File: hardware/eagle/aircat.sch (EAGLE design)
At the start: 180 parts, among them CON1 A10_OLINUXINO_LIME_SHIELD_TEM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, CON2 ANALOG_OUT, CON3 ANALOG_IN, CON4 SPDIF_OUT, U1 PCM3168A, U2 OPA1644AIPW, U3 OPA1644AIPW, U4 OPA1644AIPW, U6 LM2662M

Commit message: added test points for unused data lines
fix #7
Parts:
- added DOUT2(NC), DOUT3(NC): TPTP10SQ, testpad:TPTP10SQ
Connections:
- new net DOUT2(NC): CON1_GPIO-3.20, DOUT2(NC).TP
- new net DOUT3(NC): CON1_GPIO-3.18, DOUT3(NC).TP
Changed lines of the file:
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@@
 <attribute name="TP_SIGNAL_NAME" value=""/>
 </part>
+<part name="DOUT2(NC)" library="testpad" deviceset="TP" device="TP10SQ" value="TPTP10SQ">
+<attribute name="MF" value=""/>
+<attribute name="MPN" value=""/>
+<attribute name="OC_FARNELL" value="unknown"/>
+<attribute name="TP_SIGNAL_NAME" value=""/>
+</part>
+<part name="DOUT3(NC)" library="testpad" deviceset="TP" device="TP10SQ" value="TPTP10SQ">
+<attribute name="MF" value=""/>
+<attribute name="MPN" value=""/>
+<attribute name="OC_FARNELL" value="unknown"/>
+<attribute name="TP_SIGNAL_NAME" value=""/>
+</part>
 </parts>
 <sheets>
@@
 <attribute name="MPN" x="-238.76" y="-114.3" size="1.778" layer="96" rot="R90" display="off"/>
 </instance>
+<instance part="DOUT2(NC)" gate="G$1" x="-157.48" y="-27.94" smashed="yes" rot="R270">
+<attribute name="OC_FARNELL" x="-157.48" y="-27.94" size="1.778" layer="96" display="off"/>
+<attribute name="MF" x="-157.48" y="-27.94" size="1.778" layer="96" display="off"/>
+<attribute name="MPN" x="-157.48" y="-27.94" size="1.778" layer="96" display="off"/>
+<attribute name="NAME" x="-156.718" y="-28.956" size="1.778" layer="95"/>
+<attribute name="TP_SIGNAL_NAME" x="-158.75" y="-29.21" size="1.778" layer="97" rot="R270"/>
+</instance>
+<instance part="DOUT3(NC)" gate="G$1" x="-157.48" y="-30.48" smashed="yes" rot="R270">
+<attribute name="OC_FARNELL" x="-157.48" y="-30.48" size="1.778" layer="96" display="off"/>
+<attribute name="MF" x="-157.48" y="-30.48" size="1.778" layer="96" display="off"/>
+<attribute name="MPN" x="-157.48" y="-30.48" size="1.778" layer="96" display="off"/>
+<attribute name="NAME" x="-156.718" y="-31.496" size="1.778" layer="95"/>
+<attribute name="TP_SIGNAL_NAME" x="-158.75" y="-31.75" size="1.778" layer="97" rot="R270"/>
+</instance>
 </instances>
 <busses>
@@
 </segment>
 </net>
+<net name="DOUT2(NC)" class="0">
+<segment>
+<pinref part="CON1" gate="_GPIO-3" pin="20"/>
+<wire x1="-182.88" y1="-27.94" x2="-180.34" y2="-27.94" width="0.1524" layer="91"/>
+<label x="-180.34" y="-27.94" size="1.778" layer="95"/>
+</segment>
+<segment>
+<pinref part="DOUT2(NC)" gate="G$1" pin="TP"/>
+<wire x1="-160.02" y1="-27.94" x2="-162.56" y2="-27.94" width="0.1524" layer="91"/>
+</segment>
+</net>
+<net name="DOUT3(NC)" class="0">
+<segment>
+<pinref part="CON1" gate="_GPIO-3" pin="18"/>
+<wire x1="-182.88" y1="-30.48" x2="-180.34" y2="-30.48" width="0.1524" layer="91"/>
+<label x="-180.34" y="-30.48" size="1.778" layer="95"/>
+</segment>
+<segment>
+<pinref part="DOUT3(NC)" gate="G$1" pin="TP"/>
+<wire x1="-160.02" y1="-30.48" x2="-162.56" y2="-30.48" width="0.1524" layer="91"/>
+</segment>
+</net>

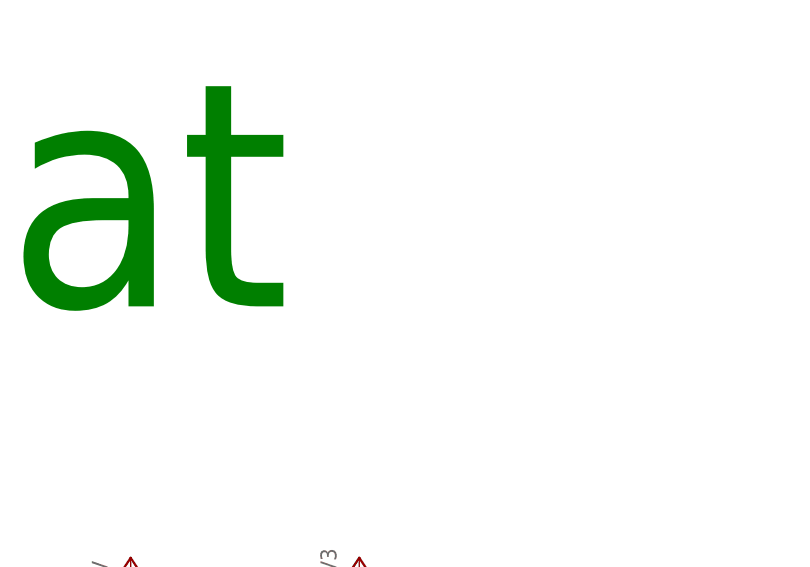
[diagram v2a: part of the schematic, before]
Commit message: added licence logo
fix #6
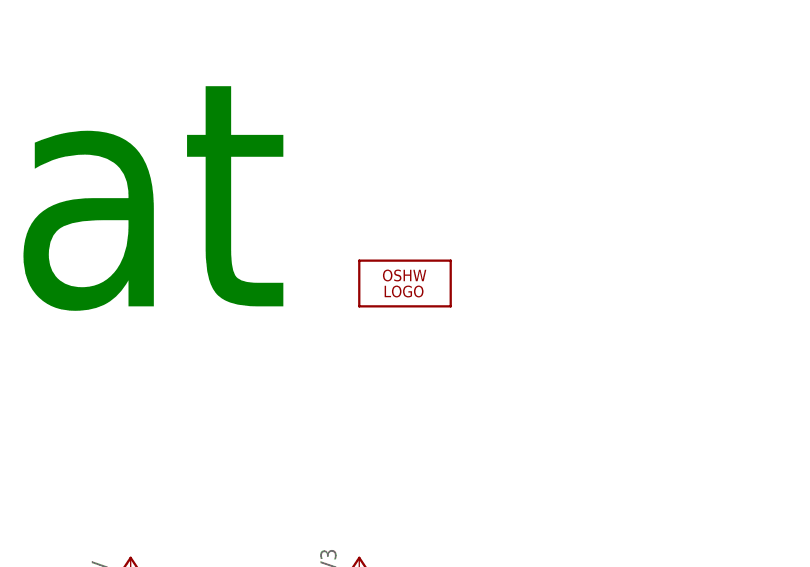
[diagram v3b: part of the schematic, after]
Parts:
- added LOGO1: OSHW_LOGO_FILLX0200-NT, ohw-logo:OSHW_LOGO_FILLX0200-NT
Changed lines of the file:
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@@
 <layer number="98" name="Guide" color="6" fill="1" visible="yes" active="yes"/>
 <layer number="100" name="Muster" color="7" fill="1" visible="no" active="no"/>
+<layer number="101" name="DRAWREF" color="11" fill="1" visible="no" active="yes"/>
+<layer number="102" name="Vscore" color="7" fill="1" visible="yes" active="yes"/>
+<layer number="103" name="tMap" color="7" fill="1" visible="yes" active="yes"/>
+<layer number="104" name="Name" color="16" fill="1" visible="yes" active="yes"/>
+<layer number="105" name="tPlate" color="7" fill="1" visible="yes" active="yes"/>
+<layer number="106" name="bPlate" color="7" fill="1" visible="yes" active="yes"/>
+<layer number="107" name="Crop" color="7" fill="1" visible="yes" active="yes"/>
+<layer number="116" name="Patch_BOT" color="9" fill="4" visible="yes" active="yes"/>
+<layer number="121" name="_tsilk" color="7" fill="1" visible="yes" active="yes"/>
+<layer number="122" name="_bsilk" color="7" fill="1" visible="yes" active="yes"/>
+<layer number="144" name="DrillLegend" color="7" fill="1" visible="no" active="yes"/>
+<layer number="151" name="HeatSink" color="7" fill="1" visible="yes" active="yes"/>
+<layer number="200" name="200bmp" color="1" fill="10" visible="no" active="yes"/>
+<layer number="201" name="201bmp" color="2" fill="10" visible="no" active="yes"/>
+<layer number="202" name="202bmp" color="3" fill="10" visible="no" active="yes"/>
+<layer number="203" name="203bmp" color="4" fill="10" visible="no" active="yes"/>
+<layer number="204" name="204bmp" color="5" fill="10" visible="no" active="yes"/>
+<layer number="205" name="205bmp" color="6" fill="10" visible="no" active="yes"/>
+<layer number="206" name="206bmp" color="7" fill="10" visible="no" active="yes"/>
+<layer number="207" name="207bmp" color="15" fill="10" visible="no" active="yes"/>
+<layer number="208" name="208bmp" color="9" fill="10" visible="yes" active="yes"/>
+<layer number="209" name="209bmp" color="7" fill="1" visible="yes" active="yes"/>
+<layer number="210" name="210bmp" color="7" fill="1" visible="yes" active="yes"/>
+<layer number="211" name="211bmp" color="7" fill="1" visible="yes" active="yes"/>
+<layer number="212" name="212bmp" color="7" fill="1" visible="yes" active="yes"/>
+<layer number="213" name="213bmp" color="7" fill="1" visible="yes" active="yes"/>
+<layer number="214" name="214bmp" color="7" fill="1" visible="yes" active="yes"/>
+<layer number="215" name="215bmp" color="7" fill="1" visible="yes" active="yes"/>
+<layer number="216" name="216bmp" color="7" fill="1" visible="yes" active="yes"/>
 <layer number="250" name="Descript" color="3" fill="1" visible="no" active="no"/>
 <layer number="251" name="SMDround" color="12" fill="11" visible="no" active="no"/>
+<layer number="254" name="cooling" color="7" fill="1" visible="yes" active="yes"/>
 </layers>
 <schematic xreflabel="%F%N/%S.%C%R" xrefpart="/%S.%C%R">
@@
 <attribute name="TP_SIGNAL_NAME" value=""/>
 </part>
+<part name="LOGO1" library="ohw-logo" deviceset="OSHW_LOGO_FILL" device="X0200-NT"/>
 </parts>
 <sheets>
@@
 <attribute name="TP_SIGNAL_NAME" x="-158.75" y="-31.75" size="1.778" layer="97" rot="R270"/>
 </instance>
+<instance part="LOGO1" gate="G$1" x="-172.72" y="210.82"/>
 </instances>
 <busses>
